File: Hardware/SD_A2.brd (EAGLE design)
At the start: 100.2 x 77.7 mm, 32 parts, among them IC1 74LS245N, IC2 LM317, IC3 2716 / 2732, IC4 XC9572XL

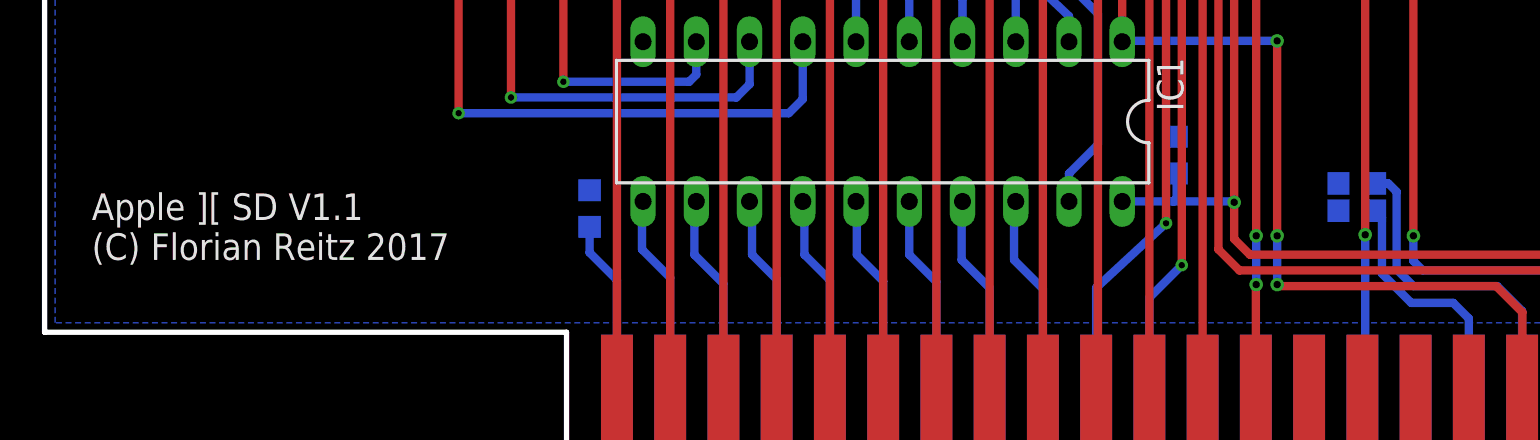
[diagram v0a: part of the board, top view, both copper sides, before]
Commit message: Schematic PDF updated
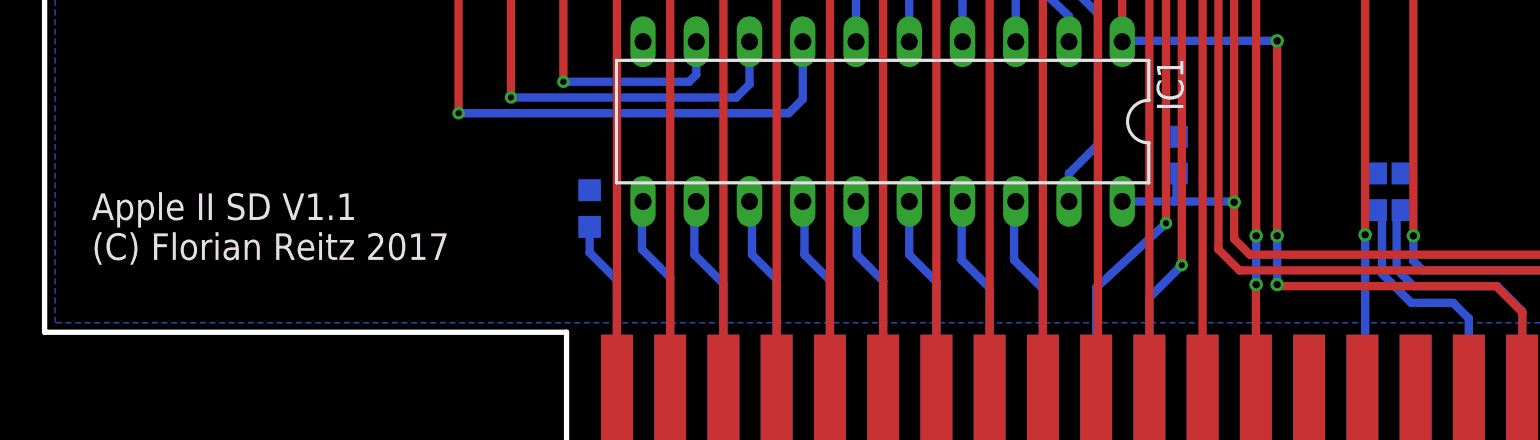
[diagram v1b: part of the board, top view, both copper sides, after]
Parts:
- moved C12 2.24 mm to (64.8, 14.5), turned to 90 degrees
- moved C13 1.27 mm to (63.5, 14.5), turned to 90 degrees
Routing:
- net -12V: track 16.1 -> 14.1 mm
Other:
- board text added: "Apple II SD V1.1 (C) Florian Reitz 2017"
- board text removed: "Apple ][ SD V1.1 (C) Florian Reitz 2017"
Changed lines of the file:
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@@
 <grid distance="0.1" unitdist="mm" unit="mm" style="dots" multiple="1" display="yes" altdistance="0.1" altunitdist="mil" altunit="mil"/>
 <layers>
-<layer number="1" name="Top" color="4" fill="1" visible="yes" active="yes"/>
+<layer number="1" name="Top" color="4" fill="1" visible="no" active="yes"/>
 <layer number="16" name="Bottom" color="1" fill="1" visible="yes" active="yes"/>
 <layer number="17" name="Pads" color="2" fill="1" visible="yes" active="yes"/>
@@
 <board>
 <plain>
-<text x="2.25" y="11.25" size="1.27" layer="25" font="vector" ratio="7">Apple ][ SD V1.1
+<text x="2.25" y="11.25" size="1.27" layer="25" font="vector" ratio="7">Apple II SD V1.1
 (C) Florian Reitz 2017</text>
 <wire x1="0" y1="7.8" x2="24.9" y2="7.8" width="0.254" layer="20"/>
@@
 <attribute name="VALUE" x="24.35" y="12.9" size="1.016" layer="28" rot="MR90"/>
 </element>
-<element name="C12" library="rcl" package="C0603K" value="100n" x="62.6" y="14.9" smashed="yes" rot="MR0">
-<attribute name="NAME" x="60.9" y="14.45" size="1.016" layer="26" rot="MR0"/>
-<attribute name="VALUE" x="63.4" y="13.25" size="1.016" layer="28" rot="MR0"/>
-</element>
-<element name="C13" library="rcl" package="C0603K" value="100n" x="62.6" y="13.6" smashed="yes" rot="MR0">
-<attribute name="NAME" x="60.9" y="13.15" size="1.016" layer="26" rot="MR0"/>
-<attribute name="VALUE" x="63.4" y="11.95" size="1.016" layer="28" rot="MR0"/>
+<element name="C12" library="rcl" package="C0603K" value="100n" x="64.8" y="14.5" smashed="yes" rot="MR90">
+<attribute name="NAME" x="64.35" y="16.2" size="1.016" layer="26" rot="MR90"/>
+<attribute name="VALUE" x="63.15" y="13.7" size="1.016" layer="28" rot="MR90"/>
+</element>
+<element name="C13" library="rcl" package="C0603K" value="100n" x="63.5" y="14.5" smashed="yes" rot="MR90">
+<attribute name="NAME" x="63.05" y="16.2" size="1.016" layer="26" rot="MR90"/>
+<attribute name="VALUE" x="61.85" y="13.7" size="1.016" layer="28" rot="MR90"/>
 </element>
 </elements>
@@
 <wire x1="65.3" y1="10" x2="64.5" y2="10.8" width="0.4" layer="16"/>
 <wire x1="69.3" y1="10" x2="65.3" y2="10" width="0.4" layer="16"/>
-<wire x1="64.5" y1="10.8" x2="64.5" y2="14.5" width="0.4" layer="16"/>
-<wire x1="64.5" y1="14.5" x2="64.1" y2="14.9" width="0.4" layer="16"/>
-<wire x1="64.1" y1="14.9" x2="63.475" y2="14.9" width="0.4" layer="16"/>
+<wire x1="64.5" y1="10.8" x2="64.5" y2="13.325" width="0.4" layer="16"/>
+<wire x1="64.5" y1="13.325" x2="64.8" y2="13.625" width="0.4" layer="16"/>
 </signal>
 <signal name="-5V">
@@
 <wire x1="67.2" y1="9.2" x2="65.2" y2="9.2" width="0.4" layer="16"/>
 <wire x1="65.2" y1="9.2" x2="63.8" y2="10.6" width="0.4" layer="16"/>
-<wire x1="63.8" y1="10.6" x2="63.8" y2="13.275" width="0.4" layer="16"/>
-<wire x1="63.8" y1="13.275" x2="63.475" y2="13.6" width="0.4" layer="16"/>
+<wire x1="63.8" y1="10.6" x2="63.8" y2="13.325" width="0.4" layer="16"/>
+<wire x1="63.8" y1="13.325" x2="63.5" y2="13.625" width="0.4" layer="16"/>
 </signal>
 </signals>

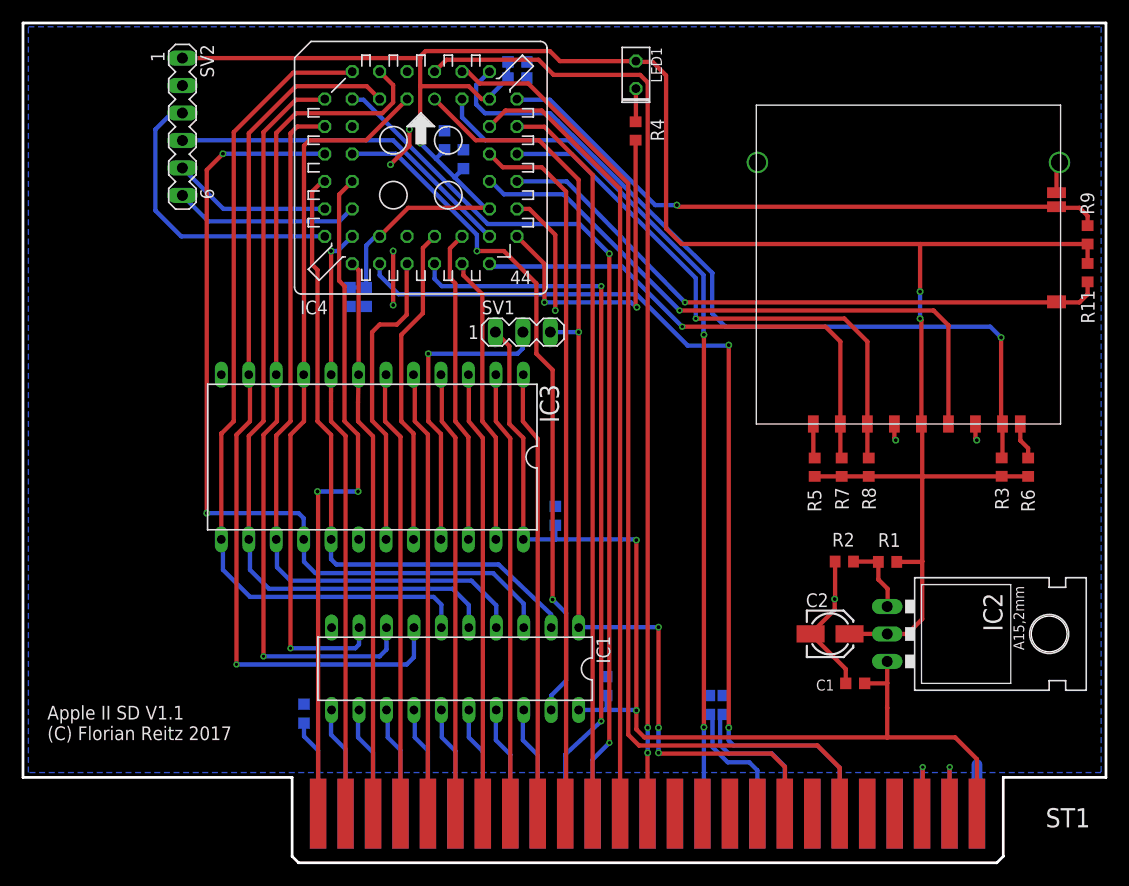
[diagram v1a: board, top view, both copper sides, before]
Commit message: NWE added to schematic and layout
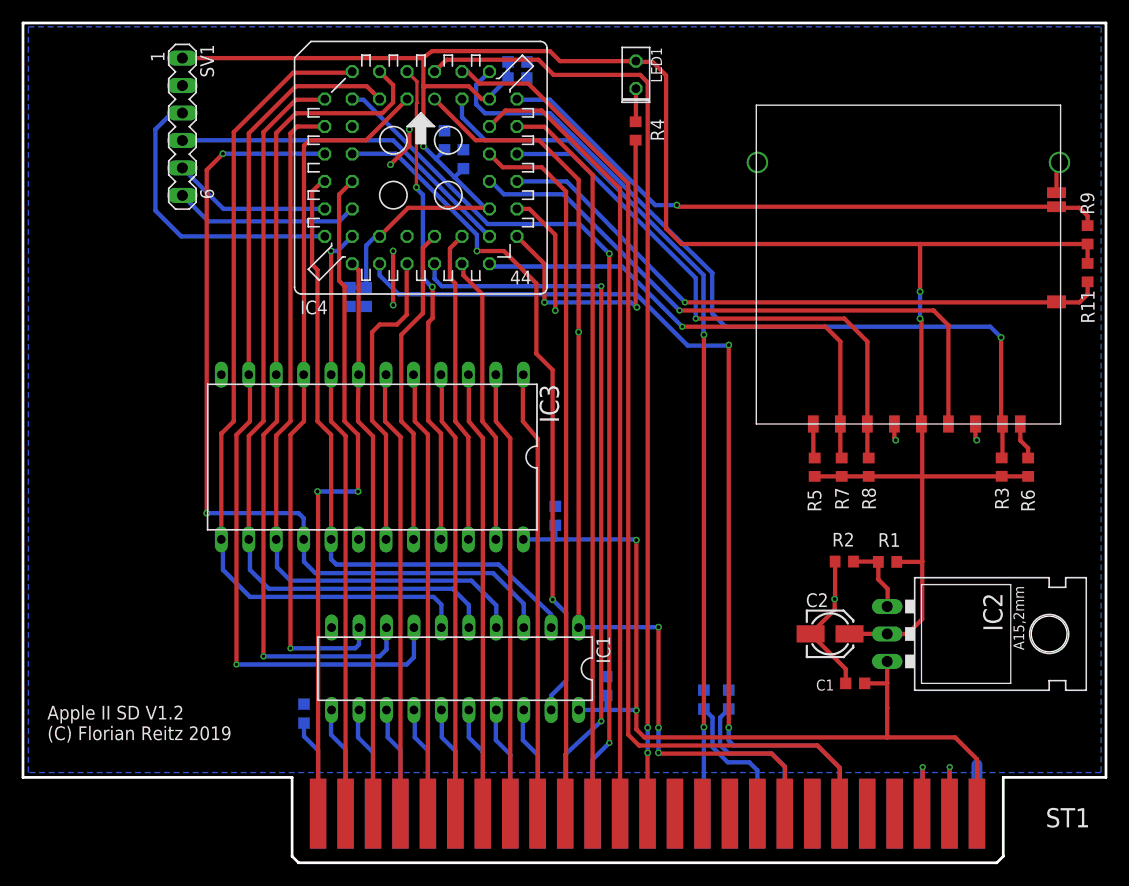
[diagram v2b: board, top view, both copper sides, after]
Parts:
- removed SV2: (no value), con-lstb:MA06-1
- SV1: device con-lstb:MA03-1 -> con-lstb:MA06-1
- moved SV1 36.8 mm to (14.8, 68.0), turned to 270 degrees
- moved C12 0.71 mm to (65.3, 15.0)
- moved C13 0.71 mm to (63.0, 15.0)
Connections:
- removed net VPP: IC3.21, SV1.2
- new net !WE: IC3.21, IC4.2
- net +3V3: now also SV1.1; no longer SV2.1
- net +5V: no longer SV1.1
- net GND: now also SV1.2; no longer SV2.2
- net R/!W: no longer SV1.3
- net TCK: now also SV1.3; no longer SV2.3
- net TDI: now also SV1.5; no longer SV2.5
- net TDO: now also SV1.4; no longer SV2.4
- net TMS: now also SV1.6; no longer SV2.6
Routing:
- net !WE: track 0.00 -> 45.0 mm, vias 0 -> 2
- net VPP: track 28.1 -> 0.00 mm, vias 1 -> 0
- net +5V: track 103.2 -> 82.9 mm
- net R/!W: track 96.2 -> 93.6 mm
- net -5V: track 12.2 -> 12.9 mm
- net -12V: track 14.1 -> 14.8 mm
- net +3V3: track 214.5 -> 214.0 mm
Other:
- board text added: "Apple II SD V1.2 (C) Florian Reitz 2019"
- board text removed: "Apple II SD V1.1 (C) Florian Reitz 2017"

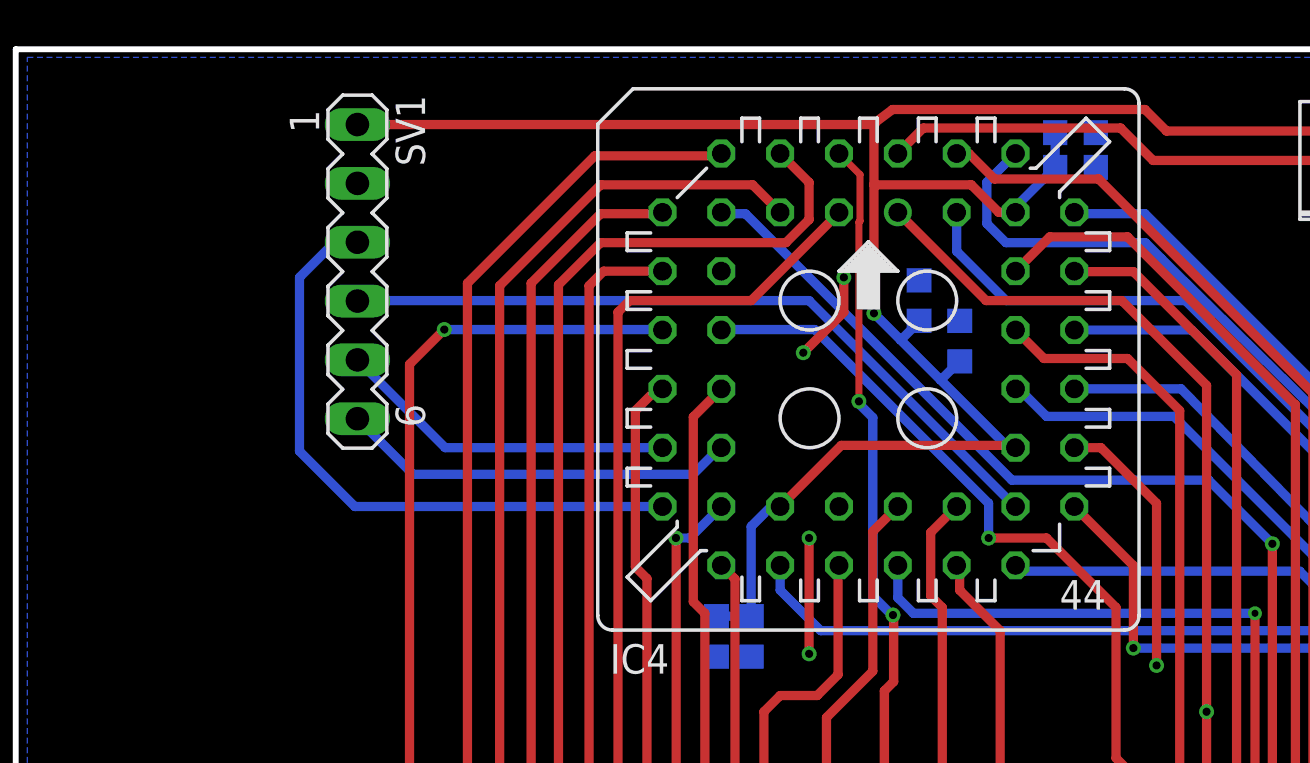
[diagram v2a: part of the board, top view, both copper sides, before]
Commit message: Tag Connect added
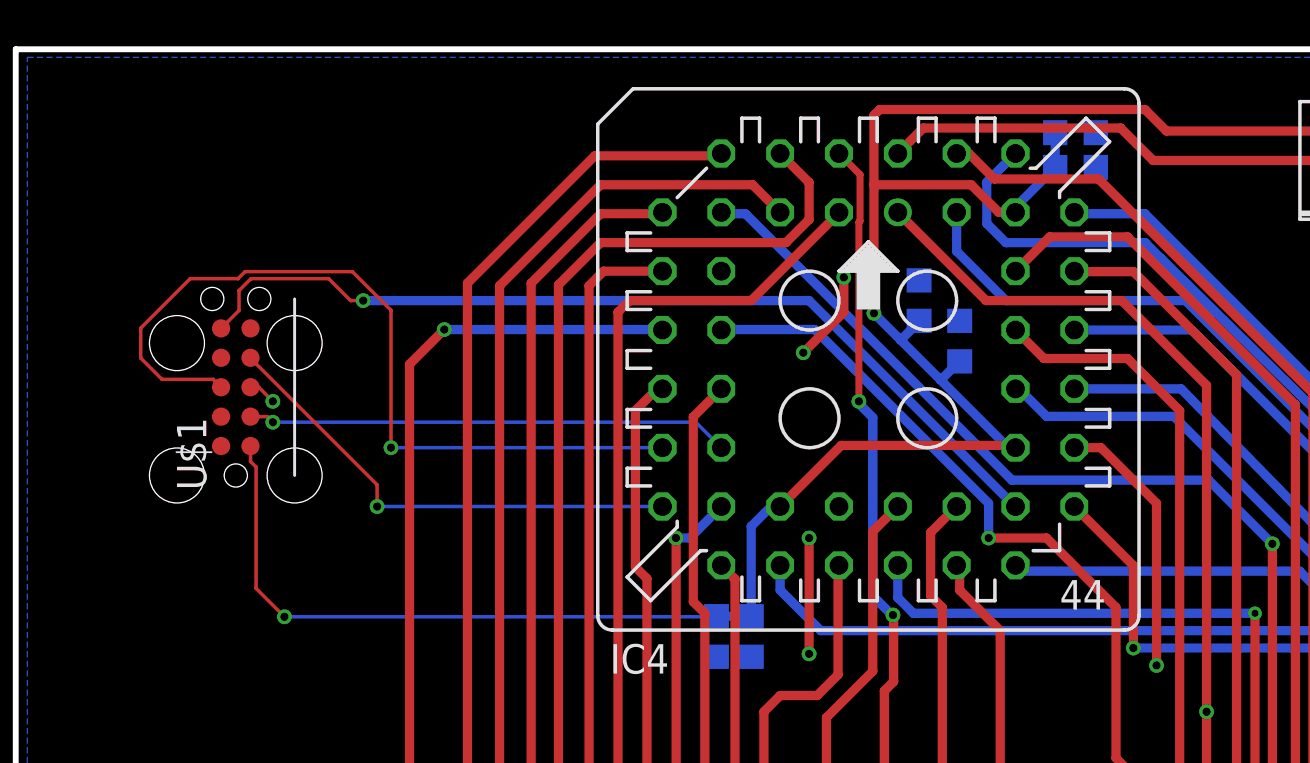
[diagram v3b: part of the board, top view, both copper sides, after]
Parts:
- removed SV1: (no value), con-lstb:MA06-1
- added U$1: TC2050-NL, eagle_tag-connect-2050:TC2050-MCP
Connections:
- net +3V3: now also U$1.1; no longer SV1.1
- net GND: now also U$1.3; no longer SV1.2
- net TCK: now also U$1.4; no longer SV1.3
- net TDI: now also U$1.8; no longer SV1.5
- net TDO: now also U$1.6; no longer SV1.4
- net TMS: now also U$1.2; no longer SV1.6
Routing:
- net TDI: track 14.7 -> 35.4 mm, vias 0 -> 1
- net TDO: track 32.1 -> 39.8 mm, vias 0 -> 1
- net TCK: track 27.3 -> 21.0 mm, vias 0 -> 1
- net +3V3: track 214.0 -> 218.6 mm, vias 3 -> 4
- net TMS: track 17.2 -> 20.9 mm, vias 0 -> 1
- net GND: track 44.8 -> 46.0 mm, vias 8 -> 9

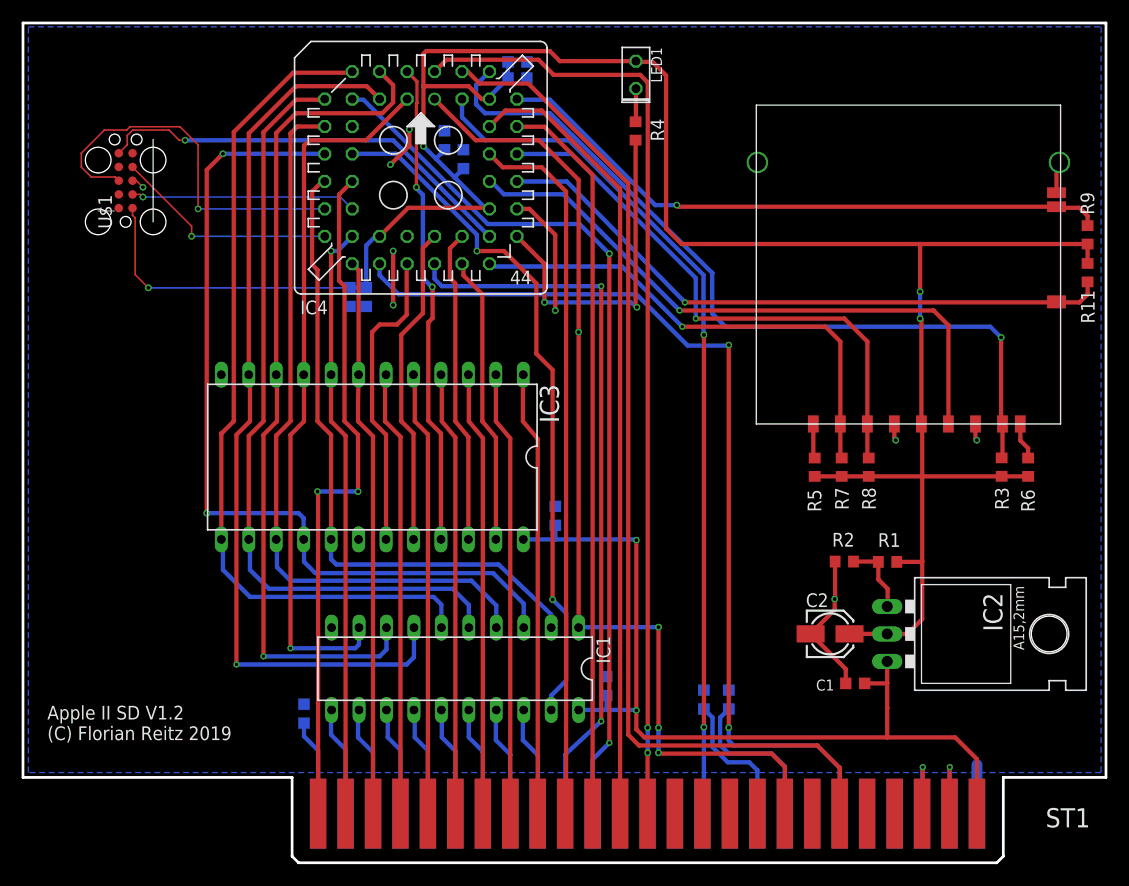
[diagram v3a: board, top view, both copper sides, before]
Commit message: EEPROM as SMD
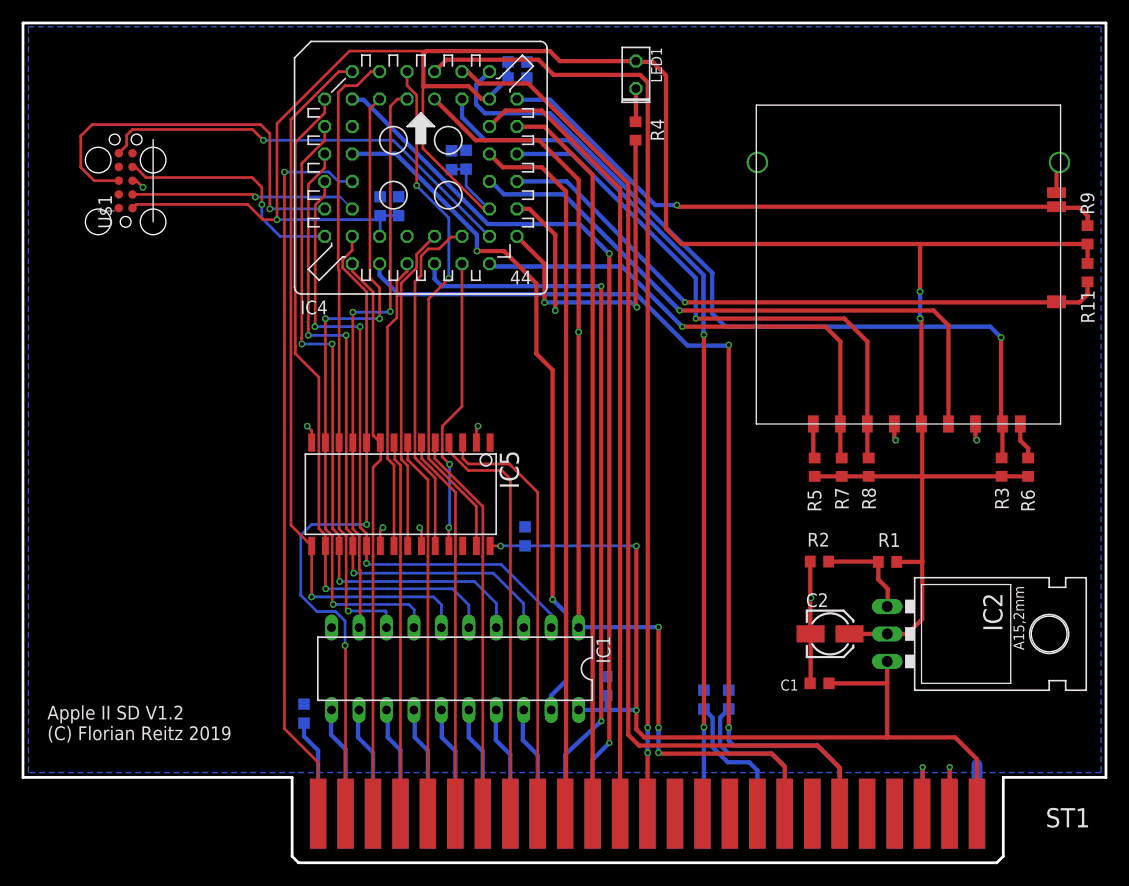
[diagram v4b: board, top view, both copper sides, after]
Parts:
- removed IC3: 2716 / 2732, memory:DIL24
- added IC5: 28C64ASO, microchip:SO28W
- moved C9 8.92 mm to (34.8, 60.6), turned to 90 degrees
- moved C6 8.85 mm to (33.0, 60.6), turned to 90 degrees
- moved C3 3.38 mm to (46.5, 30.1)
- moved C1 3.30 mm to (73.7, 16.5)
- moved C7 2.69 mm to (41.0, 65.0)
- moved R2 2.30 mm to (73.7, 27.8)
- moved C10 1.10 mm to (39.6, 64.9)
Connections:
- net N$10 renamed D6
- net N$11 renamed D5
- net N$14 renamed D4
- net N$15 renamed D3
- net N$16 renamed D2
- net N$17 renamed D1
- net N$7 renamed D0
- net N$8 renamed D7
- net !OE: now also IC5.22; no longer IC3.20
- net !WE: now also IC5.27; no longer IC3.21
- net +5V: now also IC5.28; no longer IC3.24
- net ADD0: now also IC5.10; no longer IC3.8
- net ADD1: now also IC5.9; no longer IC3.7
- net ADD2: now also IC5.8; no longer IC3.6
- net ADD3: now also IC5.7; no longer IC3.5
- net ADD4: now also IC5.6; no longer IC3.4
- net ADD5: now also IC5.5; no longer IC3.3
- net ADD6: now also IC5.4; no longer IC3.2
- net ADD7: now also IC5.3; no longer IC3.1
- net B10: now also IC5.21; no longer IC3.19
- net B8: now also IC5.25; no longer IC3.23
- net B9: now also IC5.24; no longer IC3.22
- net DATA0: now also IC5.11; no longer IC3.9
- net DATA1: now also IC5.12; no longer IC3.10
- net DATA2: now also IC5.13; no longer IC3.11
- net DATA3: now also IC5.15; no longer IC3.13
- net DATA4: now also IC5.16; no longer IC3.14
- net DATA5: now also IC5.17; no longer IC3.15
- net DATA6: now also IC5.18; no longer IC3.16
- net DATA7: now also IC5.19; no longer IC3.17
- net GND: now also IC5.14, IC5.2, IC5.20, IC5.23; no longer IC3.12, IC3.18
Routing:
- net DATA2: track 83.5 -> 62.2 mm, vias 1 -> 3
- net DATA1: track 78.0 -> 58.0 mm
- net DATA6: track 80.7 -> 62.3 mm, vias 2 -> 3
- net DATA0: track 66.4 -> 53.8 mm, vias 1 -> 2
- net +3V3: track 218.6 -> 230.4 mm, vias 4 -> 3
- net DATA3: track 78.0 -> 66.9 mm, vias 0 -> 1
- net DATA4: track 71.7 -> 63.6 mm, vias 0 -> 1
- net ADD0: track 55.1 -> 62.9 mm, vias 1 -> 2
- net ADD2: track 41.2 -> 34.6 mm
- net ADD3: track 41.2 -> 35.1 mm
- net ADD4: track 41.1 -> 35.6 mm
- net ADD5: track 41.1 -> 36.2 mm
- net GND: track 46.0 -> 41.5 mm
- net +5V: track 82.9 -> 87.4 mm, vias 2 -> 3
- net DATA5: track 68.0 -> 63.6 mm, vias 0 -> 3
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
